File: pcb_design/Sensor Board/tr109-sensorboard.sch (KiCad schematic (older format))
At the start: 52 parts, among them J1 Conn_01x01_Female, J2 Conn_01x01_Female, J47 Raspberry_Pi_2_3, U1 BME680, U2 74HC595, U2 LIS3MDLTR, U3 AMG8833

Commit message: cleanup and revisions
changes to the sensor and main boards
clean up of the blender file to remove some deprecated meshes
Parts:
- renumbered U2 to U4
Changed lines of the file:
@@
 3.3V
 $Comp
-L dk_Magnetic-Sensors-Linear-Compass-ICs:LIS3MDLTR U2
+L dk_Magnetic-Sensors-Linear-Compass-ICs:LIS3MDLTR U4
 U 1 1 5F5C68D1
 P 4200 1700
-F 0 "U2" H 3550 2400 60  0000 C CNN
+F 0 "U4" H 3550 2400 60  0000 C CNN
 F 1 "LIS3MDLTR" H 3700 2300 60  0000 C CNN
 F 2 "digikey-footprints:VFLGA-12_2x2mm" H 4400 1900 60  0001 L CNN

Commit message: sensor board revisions
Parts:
- removed U4: LIS3MDLTR, digikey-footprints:VFLGA-12_2x2mm, symbol dk_Magnetic-Sensors-Linear-Compass-ICs:LIS3MDLTR
- added J3: Conn_01x04_Female, Connector_PinHeader_1.00mm:PinHeader_1x04_P1.00mm_Vertical, symbol Connector:Conn_01x04_Female
- J1, J2: footprint Connector_Wire:SolderWirePad_1x01_SMD_1x2mm -> TestPoint:TestPoint_Pad_1.0x1.0mm
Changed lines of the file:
@@
 Text GLabel 5850 1500 0    50   Input ~ 0
 3.3V
-Text GLabel 3700 1900 0    50   Input ~ 0
-SDA
-Text GLabel 3700 1600 0    50   Input ~ 0
-SCK
-Text GLabel 4100 2300 3    50   Input ~ 0
-GND
-Text GLabel 4200 1200 1    50   Input ~ 0
-3.3V
-$Comp
-L dk_Magnetic-Sensors-Linear-Compass-ICs:LIS3MDLTR U4
-U 1 1 5F5C68D1
-P 4200 1700
-F 0 "U4" H 3550 2400 60  0000 C CNN
-F 1 "LIS3MDLTR" H 3700 2300 60  0000 C CNN
-F 2 "digikey-footprints:VFLGA-12_2x2mm" H 4400 1900 60  0001 L CNN
-F 3 "http://www.st.com/content/ccc/resource/technical/document/datasheet/54/2a/85/76/e3/97/42/18/DM00075867.pdf/files/DM00075867.pdf/jcr:content/translations/en.DM00075867.pdf" H 4400 2000 60  0001 L CNN
-F 4 "497-13892-1-ND" H 4400 2100 60  0001 L CNN "Digi-Key_PN"
-F 5 "LIS3MDLTR" H 4400 2200 60  0001 L CNN "MPN"
-F 6 "Sensors, Transducers" H 4400 2300 60  0001 L CNN "Category"
-F 7 "Magnetic Sensors - Linear, Compass (ICs)" H 4400 2400 60  0001 L CNN "Family"
-F 8 "http://www.st.com/content/ccc/resource/technical/document/datasheet/54/2a/85/76/e3/97/42/18/DM00075867.pdf/files/DM00075867.pdf/jcr:content/translations/en.DM00075867.pdf" H 4400 2500 60  0001 L CNN "DK_Datasheet_Link"
-F 9 "/product-detail/en/stmicroelectronics/LIS3MDLTR/497-13892-1-ND/4309737" H 4400 2600 60  0001 L CNN "DK_Detail_Page"
-F 10 "SENSOR MR I2C/SPI 12LGA" H 4400 2700 60  0001 L CNN "Description"
-F 11 "STMicroelectronics" H 4400 2800 60  0001 L CNN "Manufacturer"
-F 12 "Active" H 4400 2900 60  0001 L CNN "Status"
-	1    4200 1700
-	1    0    0    -1
-$EndComp
 Text GLabel 4550 6400 2    50   Input ~ 0
 GND
@@
 F 0 "J2" H 5728 5626 50  0000 L CNN
 F 1 "Conn_01x01_Female" H 5728 5535 50  0000 L CNN
-F 2 "Connector_Wire:SolderWirePad_1x01_SMD_1x2mm" H 5700 5600 50  0001 C CNN
+F 2 "TestPoint:TestPoint_Pad_1.0x1.0mm" H 5700 5600 50  0001 C CNN
 F 3 "~" H 5700 5600 50  0001 C CNN
 	1    5700 5600
@@
 F 0 "J1" H 5728 5276 50  0000 L CNN
 F 1 "Conn_01x01_Female" H 5728 5185 50  0000 L CNN
-F 2 "Connector_Wire:SolderWirePad_1x01_SMD_1x2mm" H 5700 5250 50  0001 C CNN
+F 2 "TestPoint:TestPoint_Pad_1.0x1.0mm" H 5700 5250 50  0001 C CNN
 F 3 "~" H 5700 5250 50  0001 C CNN
 	1    5700 5250
@@
 Text GLabel 6750 1600 2    50   Input ~ 0
 GND
+$Comp
+L Connector:Conn_01x04_Female J3
+U 1 1 60B3C235
+P 3900 1550
+F 0 "J3" H 3928 1526 50  0000 L CNN
+F 1 "Conn_01x04_Female" H 3928 1435 50  0000 L CNN
+F 2 "Connector_PinHeader_1.00mm:PinHeader_1x04_P1.00mm_Vertical" H 3900 1550 50  0001 C CNN
+F 3 "~" H 3900 1550 50  0001 C CNN
+	1    3900 1550
+	1    0    0    -1
+$EndComp
+Text GLabel 3700 1450 0    50   Input ~ 0
+SDA
+Text GLabel 3700 1750 0    50   Input ~ 0
+SCK
+Text GLabel 3700 1550 0    50   Input ~ 0
+3.3V
+Text GLabel 3700 1650 0    50   Input ~ 0
+GND
 $EndSCHEMATC

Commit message: sensor board schematic
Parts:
- J3: footprint Connector_PinHeader_1.00mm:PinHeader_1x04_P1.00mm_Vertical -> Connector_PinHeader_2.54mm:PinHeader_1x04_P2.54mm_Vertical
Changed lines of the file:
@@
 F 0 "J3" H 3928 1526 50  0000 L CNN
 F 1 "Conn_01x04_Female" H 3928 1435 50  0000 L CNN
-F 2 "Connector_PinHeader_1.00mm:PinHeader_1x04_P1.00mm_Vertical" H 3900 1550 50  0001 C CNN
+F 2 "Connector_PinHeader_2.54mm:PinHeader_1x04_P2.54mm_Vertical" H 3900 1550 50  0001 C CNN
 F 3 "~" H 3900 1550 50  0001 C CNN
 	1    3900 1550

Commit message: Pcb and shell design work
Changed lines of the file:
@@
 Text GLabel 1750 2800 1    50   Input ~ 0
 5V
-Text GLabel 1150 4000 0    50   Input ~ 0
+Text GLabel 1150 4700 0    50   Input ~ 0
 Shift_Clock
-Text GLabel 2750 4000 2    50   Input ~ 0
+Text GLabel 1150 4100 0    50   Input ~ 0
 Shift_Latch
 Wire Wire Line
@@
 Text GLabel 9100 5350 0    50   Input ~ 0
 GND
-Text GLabel 1150 3500 0    50   Input ~ 0
+Text GLabel 1150 3900 0    50   Input ~ 0
 Shift_Serial
 Text GLabel 6750 1600 2    50   Input ~ 0

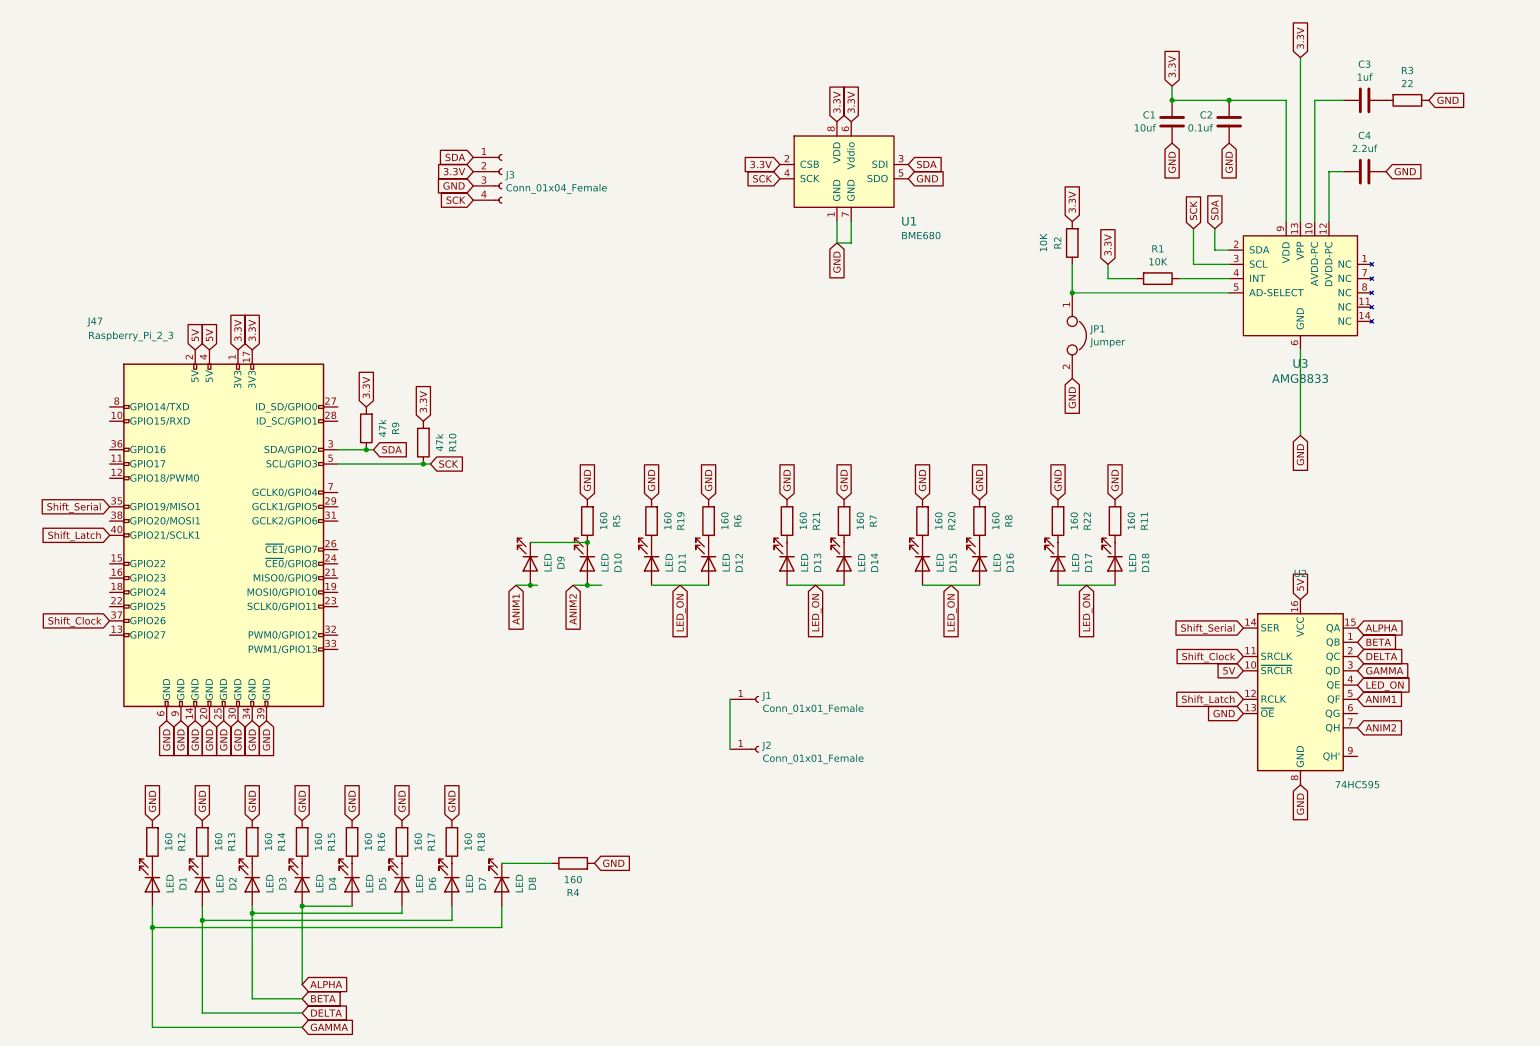
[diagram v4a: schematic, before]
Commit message: Rev 3 board changes, blender file changes
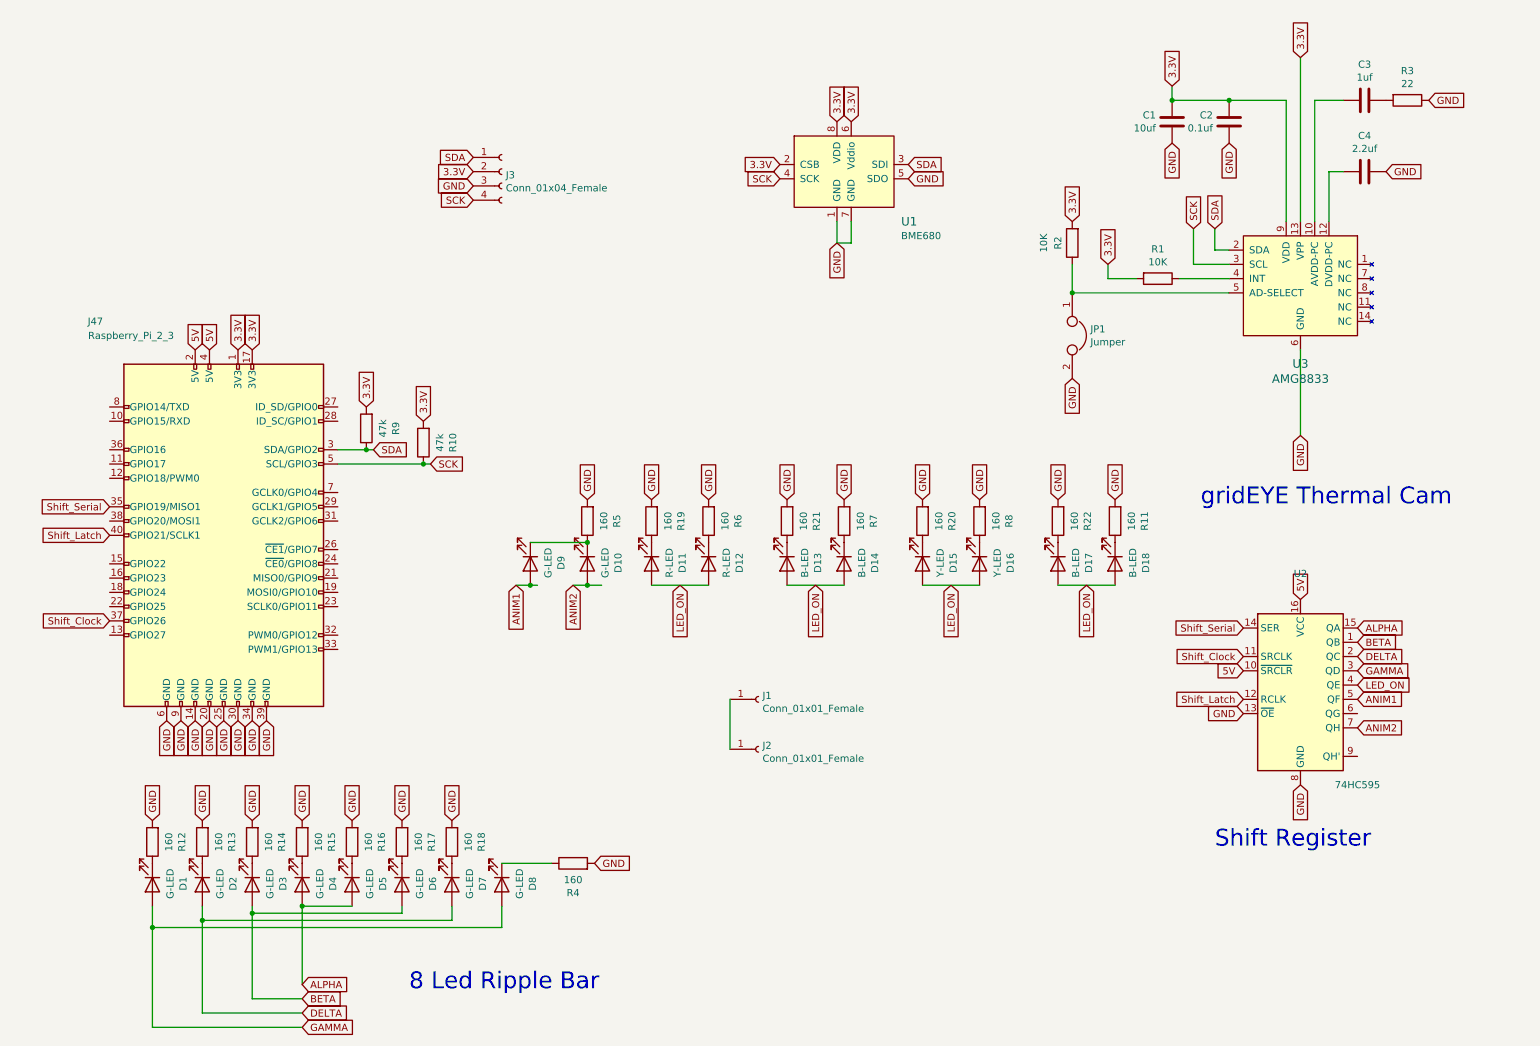
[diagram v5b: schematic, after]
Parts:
- D1, D10, D2, D3, D4, D5, D6, D7, D8, D9: value LED -> G-LED
- D11, D12: value LED -> R-LED
- D13, D14, D17, D18: value LED -> B-LED
- D15, D16: value LED -> Y-LED
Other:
- note added: "8 Led Ripple Bar"
- note added: "Shift Register"
- note added: "gridEYE Thermal Cam"
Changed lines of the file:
@@
 P 4100 4300
 F 0 "D9" H 4093 4516 50  0000 C CNN
-F 1 "LED" H 4093 4425 50  0000 C CNN
+F 1 "G-LED" H 4093 4425 50  0000 C CNN
 F 2 "LED_SMD:LED_1206_3216Metric_Pad1.42x1.75mm_HandSolder" H 4100 4300 50  0001 C CNN
 F 3 "~" H 4100 4300 50  0001 C CNN
@@
 P 4500 4300
 F 0 "D10" H 4493 4516 50  0000 C CNN
-F 1 "LED" H 4493 4425 50  0000 C CNN
+F 1 "G-LED" H 4493 4425 50  0000 C CNN
 F 2 "LED_SMD:LED_1206_3216Metric_Pad1.42x1.75mm_HandSolder" H 4500 4300 50  0001 C CNN
 F 3 "~" H 4500 4300 50  0001 C CNN
@@
 P 5350 4300
 F 0 "D12" H 5343 4516 50  0000 C CNN
-F 1 "LED" H 5343 4425 50  0000 C CNN
+F 1 "R-LED" H 5343 4425 50  0000 C CNN
 F 2 "LED_SMD:LED_1206_3216Metric_Pad1.42x1.75mm_HandSolder" H 5350 4300 50  0001 C CNN
 F 3 "~" H 5350 4300 50  0001 C CNN
@@
 P 4950 4300
 F 0 "D11" H 4943 4516 50  0000 C CNN
-F 1 "LED" H 4943 4425 50  0000 C CNN
+F 1 "R-LED" H 4943 4425 50  0000 C CNN
 F 2 "LED_SMD:LED_1206_3216Metric_Pad1.42x1.75mm_HandSolder" H 4950 4300 50  0001 C CNN
 F 3 "~" H 4950 4300 50  0001 C CNN
@@
 P 6300 4300
 F 0 "D14" H 6293 4516 50  0000 C CNN
-F 1 "LED" H 6293 4425 50  0000 C CNN
+F 1 "B-LED" H 6293 4425 50  0000 C CNN
 F 2 "LED_SMD:LED_1206_3216Metric_Pad1.42x1.75mm_HandSolder" H 6300 4300 50  0001 C CNN
 F 3 "~" H 6300 4300 50  0001 C CNN
@@
 P 5900 4300
 F 0 "D13" H 5893 4516 50  0000 C CNN
-F 1 "LED" H 5893 4425 50  0000 C CNN
+F 1 "B-LED" H 5893 4425 50  0000 C CNN
 F 2 "LED_SMD:LED_1206_3216Metric_Pad1.42x1.75mm_HandSolder" H 5900 4300 50  0001 C CNN
 F 3 "~" H 5900 4300 50  0001 C CNN
@@
 P 7250 4300
 F 0 "D16" H 7243 4516 50  0000 C CNN
-F 1 "LED" H 7243 4425 50  0000 C CNN
+F 1 "Y-LED" H 7243 4425 50  0000 C CNN
 F 2 "LED_SMD:LED_1206_3216Metric_Pad1.42x1.75mm_HandSolder" H 7250 4300 50  0001 C CNN
 F 3 "~" H 7250 4300 50  0001 C CNN
@@
 P 6850 4300
 F 0 "D15" H 6843 4516 50  0000 C CNN
-F 1 "LED" H 6843 4425 50  0000 C CNN
+F 1 "Y-LED" H 6843 4425 50  0000 C CNN
 F 2 "LED_SMD:LED_1206_3216Metric_Pad1.42x1.75mm_HandSolder" H 6850 4300 50  0001 C CNN
 F 3 "~" H 6850 4300 50  0001 C CNN
@@
 P 8200 4300
 F 0 "D18" H 8193 4516 50  0000 C CNN
-F 1 "LED" H 8193 4425 50  0000 C CNN
+F 1 "B-LED" H 8193 4425 50  0000 C CNN
 F 2 "LED_SMD:LED_1206_3216Metric_Pad1.42x1.75mm_HandSolder" H 8200 4300 50  0001 C CNN
 F 3 "~" H 8200 4300 50  0001 C CNN
@@
 P 7800 4300
 F 0 "D17" H 7793 4516 50  0000 C CNN
-F 1 "LED" H 7793 4425 50  0000 C CNN
+F 1 "B-LED" H 7793 4425 50  0000 C CNN
 F 2 "LED_SMD:LED_1206_3216Metric_Pad1.42x1.75mm_HandSolder" H 7800 4300 50  0001 C CNN
 F 3 "~" H 7800 4300 50  0001 C CNN
@@
 P 3900 6550
 F 0 "D8" H 3893 6766 50  0000 C CNN
-F 1 "LED" H 3893 6675 50  0000 C CNN
+F 1 "G-LED" H 3893 6675 50  0000 C CNN
 F 2 "LED_SMD:LED_1206_3216Metric_Pad1.42x1.75mm_HandSolder" H 3900 6550 50  0001 C CNN
 F 3 "~" H 3900 6550 50  0001 C CNN
@@
 P 3550 6550
 F 0 "D7" H 3543 6766 50  0000 C CNN
-F 1 "LED" H 3543 6675 50  0000 C CNN
+F 1 "G-LED" H 3543 6675 50  0000 C CNN
 F 2 "LED_SMD:LED_1206_3216Metric_Pad1.42x1.75mm_HandSolder" H 3550 6550 50  0001 C CNN
 F 3 "~" H 3550 6550 50  0001 C CNN
@@
 P 1450 6550
 F 0 "D1" H 1443 6766 50  0000 C CNN
-F 1 "LED" H 1443 6675 50  0000 C CNN
+F 1 "G-LED" H 1443 6675 50  0000 C CNN
 F 2 "LED_SMD:LED_1206_3216Metric_Pad1.42x1.75mm_HandSolder" H 1450 6550 50  0001 C CNN
 F 3 "~" H 1450 6550 50  0001 C CNN
@@
 P 1800 6550
 F 0 "D2" H 1793 6766 50  0000 C CNN
-F 1 "LED" H 1793 6675 50  0000 C CNN
+F 1 "G-LED" H 1793 6675 50  0000 C CNN
 F 2 "LED_SMD:LED_1206_3216Metric_Pad1.42x1.75mm_HandSolder" H 1800 6550 50  0001 C CNN
 F 3 "~" H 1800 6550 50  0001 C CNN
@@
 P 3200 6550
 F 0 "D6" H 3193 6766 50  0000 C CNN
-F 1 "LED" H 3193 6675 50  0000 C CNN
+F 1 "G-LED" H 3193 6675 50  0000 C CNN
 F 2 "LED_SMD:LED_1206_3216Metric_Pad1.42x1.75mm_HandSolder" H 3200 6550 50  0001 C CNN
 F 3 "~" H 3200 6550 50  0001 C CNN
@@
 P 2850 6550
 F 0 "D5" H 2843 6766 50  0000 C CNN
-F 1 "LED" H 2843 6675 50  0000 C CNN
+F 1 "G-LED" H 2843 6675 50  0000 C CNN
 F 2 "LED_SMD:LED_1206_3216Metric_Pad1.42x1.75mm_HandSolder" H 2850 6550 50  0001 C CNN
 F 3 "~" H 2850 6550 50  0001 C CNN
@@
 P 2500 6550
 F 0 "D4" H 2493 6766 50  0000 C CNN
-F 1 "LED" H 2493 6675 50  0000 C CNN
+F 1 "G-LED" H 2493 6675 50  0000 C CNN
 F 2 "LED_SMD:LED_1206_3216Metric_Pad1.42x1.75mm_HandSolder" H 2500 6550 50  0001 C CNN
 F 3 "~" H 2500 6550 50  0001 C CNN
@@
 P 2150 6550
 F 0 "D3" H 2143 6766 50  0000 C CNN
-F 1 "LED" H 2143 6675 50  0000 C CNN
+F 1 "G-LED" H 2143 6675 50  0000 C CNN
 F 2 "LED_SMD:LED_1206_3216Metric_Pad1.42x1.75mm_HandSolder" H 2150 6550 50  0001 C CNN
 F 3 "~" H 2150 6550 50  0001 C CNN
@@
 Text GLabel 3700 1650 0    50   Input ~ 0
 GND
+Text Notes 3250 7300 0    118  ~ 0
+8 Led Ripple Bar
+Text Notes 8900 6300 0    118  ~ 0
+Shift Register
+Text Notes 8800 3900 0    118  ~ 0
+gridEYE Thermal Cam
 $EndSCHEMATC

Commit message: Kicad Sheet Title Corrections
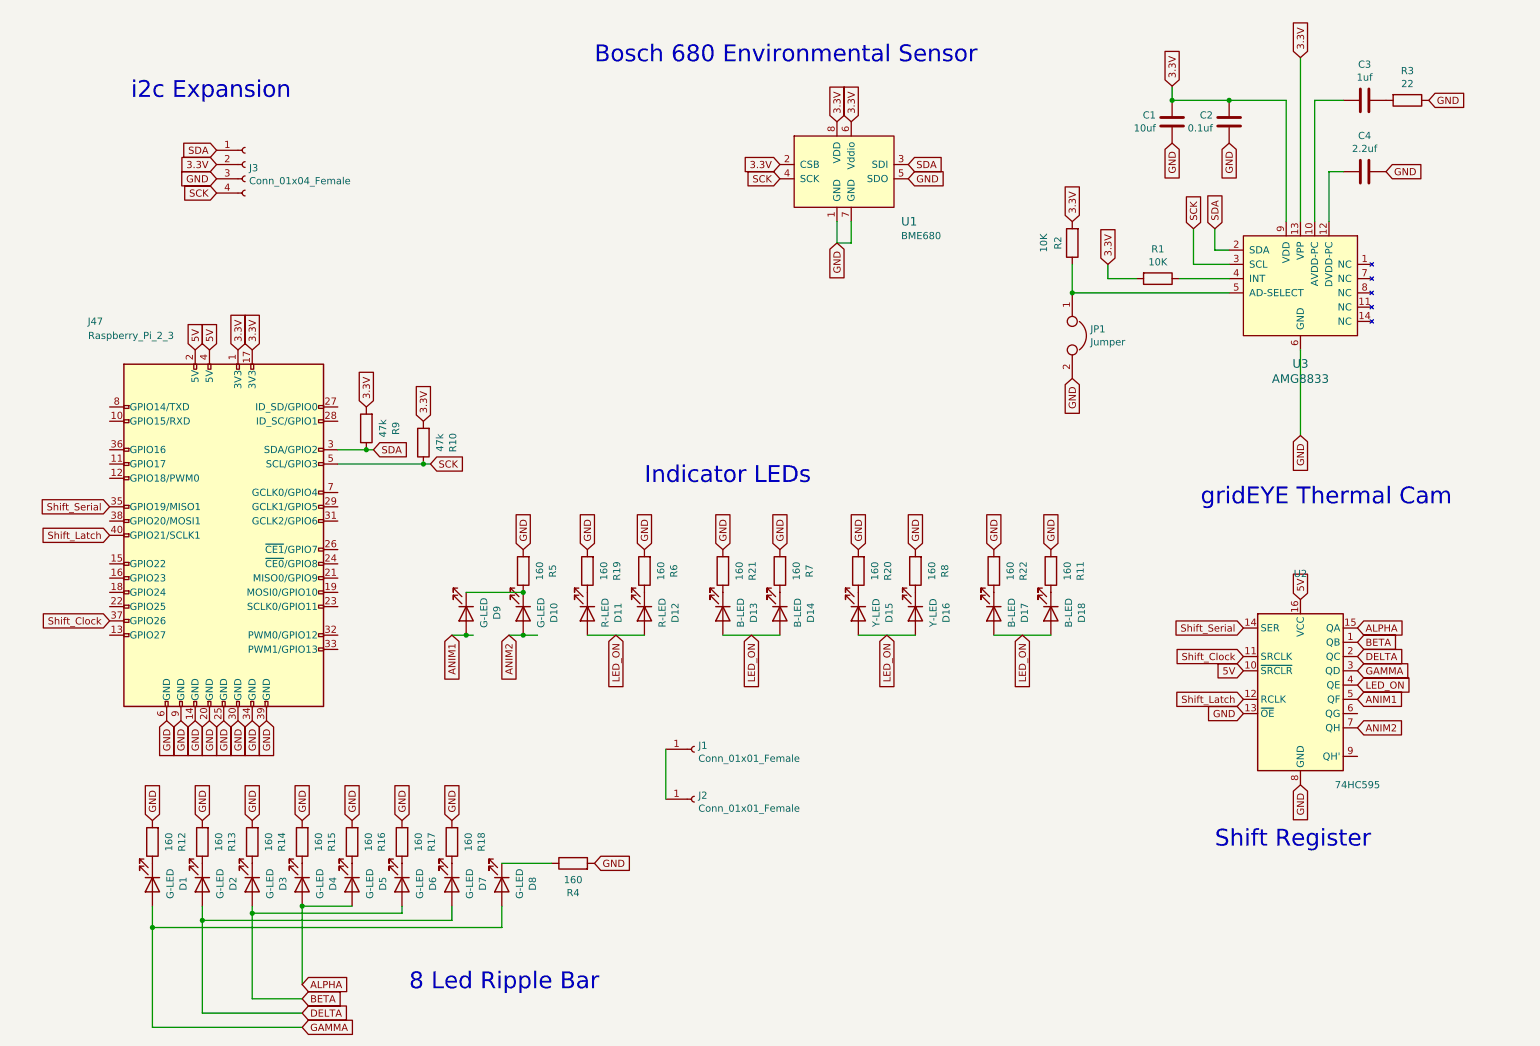
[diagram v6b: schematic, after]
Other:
- note added: "Bosch 680 Environmental Sensor\n"
- note added: "Indicator LEDs"
- note added: "i2c Expansion"
- moved on the sheet: D10, D11, D12, D13, D14, D15, D16, D17, D18, D9, J1, J2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
